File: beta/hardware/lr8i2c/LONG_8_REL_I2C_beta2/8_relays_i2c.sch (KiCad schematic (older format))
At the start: 90 parts, among them K101 G5LA-1-12VDC, K102 G5LA-1-12VDC, K103 G5LA-1-12VDC, K104 G5LA-1-12VDC, K105 G5LA-1-12VDC, K106 G5LA-1-12VDC, K107 G5LA-1-12VDC, K108 G5LA-1-12VDC, P101 CONN_3, P102 CONN_3, P103 CONN_3, P104 CONN_3, P105 CONN_3, P106 CONN_3, P107 CONN_3, P108 CONN_3, P109 CONN_2, P110 CONN_6, P112 CONN_6, Q101 PNP, Q102 PNP, Q103 PNP, Q104 PNP, Q105 PNP, Q106 PNP, Q107 PNP, Q108 PNP, Q109 DSS20201L NPN, Q110 DSS20201L NPN, Q111 DSS20201L NPN, Q112 DSS20201L NPN, Q113 DSS20201L NPN, Q114 DSS20201L NPN, Q115 DSS20201L NPN, Q116 DSS20201L NPN, U101 PCF8574

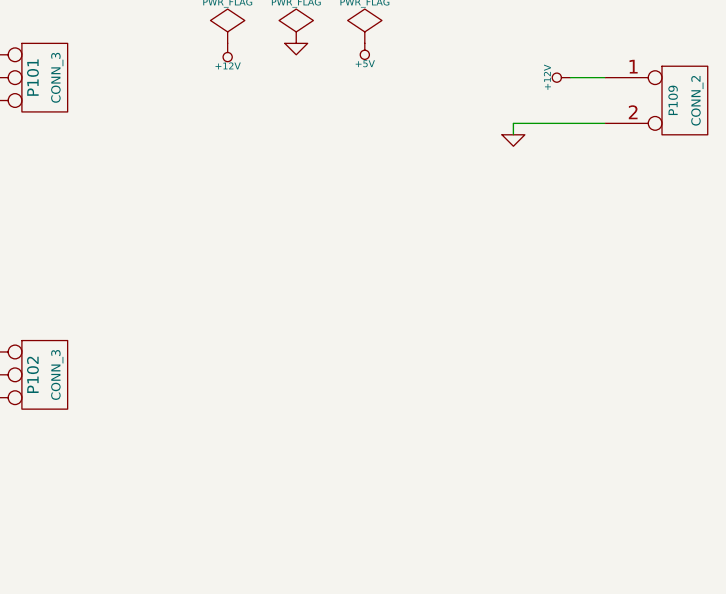
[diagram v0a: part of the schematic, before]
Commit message: ajout led presence 5v et 12v
Reste:
- trou de percage
- placement serigraphie
- verification en fonction des contraintes de fabrication (largeur piste, via...)
- logo sous face
- reference de la carte
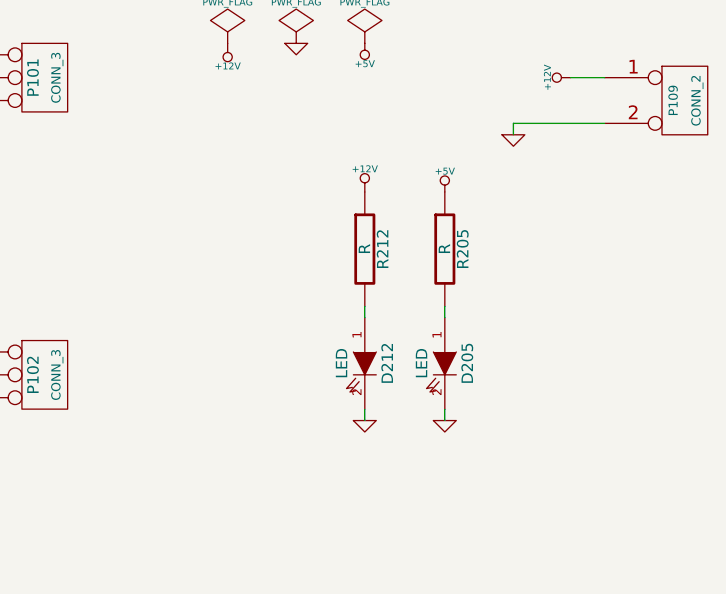
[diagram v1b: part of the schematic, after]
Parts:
- added D205, D212: LED, symbol LED
- added R205, R212: R, symbol R
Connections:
- net +12V: now also R212.1
- net +5V: now also R205.1
- net GND: now also D205.2 (K), D212.2 (K)
- new net: D212.1 (A), R212.2
- new net: D205.1 (A), R205.2
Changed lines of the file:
@@
-EESchema Schematic File Version 2  date mer. 18 avril 2012 22:31:56 CEST
+EESchema Schematic File Version 2  date 19/04/2012 10:46:38
 LIBS:power
 LIBS:device
@@
 Sheet 1 1
 Title ""
-Date "18 apr 2012"
+Date "19 apr 2012"
 Rev ""
 Comp ""
@@
 $EndDescr
 $Comp
+L +5V #PWR?
+U 1 1 4F8FD0CA
+P 13650 1550
+F 0 "#PWR?" H 13650 1640 20  0001 C CNN
+F 1 "+5V" H 13650 1640 30  0000 C CNN
+	1    13650 1550
+	1    0    0    -1
+$EndComp
+$Comp
+L +12V #PWR?
+U 1 1 4F8FD0C4
+P 13300 1550
+F 0 "#PWR?" H 13300 1500 20  0001 C CNN
+F 1 "+12V" H 13300 1650 30  0000 C CNN
+	1    13300 1550
+	1    0    0    -1
+$EndComp
+$Comp
+L GND #PWR?
+U 1 1 4F8FD0BD
+P 13300 2550
+F 0 "#PWR?" H 13300 2550 30  0001 C CNN
+F 1 "GND" H 13300 2480 30  0001 C CNN
+	1    13300 2550
+	1    0    0    -1
+$EndComp
+$Comp
+L GND #PWR?
+U 1 1 4F8FD0B0
+P 13650 2550
+F 0 "#PWR?" H 13650 2550 30  0001 C CNN
+F 1 "GND" H 13650 2480 30  0001 C CNN
+	1    13650 2550
+	1    0    0    -1
+$EndComp
+Wire Wire Line
+	13650 2100 13650 2050
+Wire Wire Line
+	13650 2500 13650 2550
+$Comp
+L LED D205
+U 1 1 4F8FD0A7
+P 13650 2300
+F 0 "D205" H 13650 2400 50  0000 C CNN
+F 1 "LED" H 13650 2200 50  0000 C CNN
+	1    13650 2300
+	0    1    1    0
+$EndComp
+$Comp
+L R R205
+U 1 1 4F8FD0A6
+P 13650 1800
+F 0 "R205" V 13730 1800 50  0000 C CNN
+F 1 "R" V 13650 1800 50  0000 C CNN
+	1    13650 1800
+	1    0    0    -1
+$EndComp
+$Comp
+L R R212
+U 1 1 4F8FD09A
+P 13300 1800
+F 0 "R212" V 13380 1800 50  0000 C CNN
+F 1 "R" V 13300 1800 50  0000 C CNN
+	1    13300 1800
+	1    0    0    -1
+$EndComp
+$Comp
+L LED D212
+U 1 1 4F8FD099
+P 13300 2300
+F 0 "D212" H 13300 2400 50  0000 C CNN
+F 1 "LED" H 13300 2200 50  0000 C CNN
+	1    13300 2300
+	0    1    1    0
+$EndComp
+Wire Wire Line
+	13300 2500 13300 2550
+Wire Wire Line
+	13300 2100 13300 2050
+$Comp
 L +5V #PWR01
